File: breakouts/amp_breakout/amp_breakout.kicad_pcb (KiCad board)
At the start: 2 copper layers, 20 parts, among them P1 CONN_01X02, U1 CONN_SMA, U2 MGA-82563, U3 ADM7150, U4 CONN_SMA, U5 mounting_box

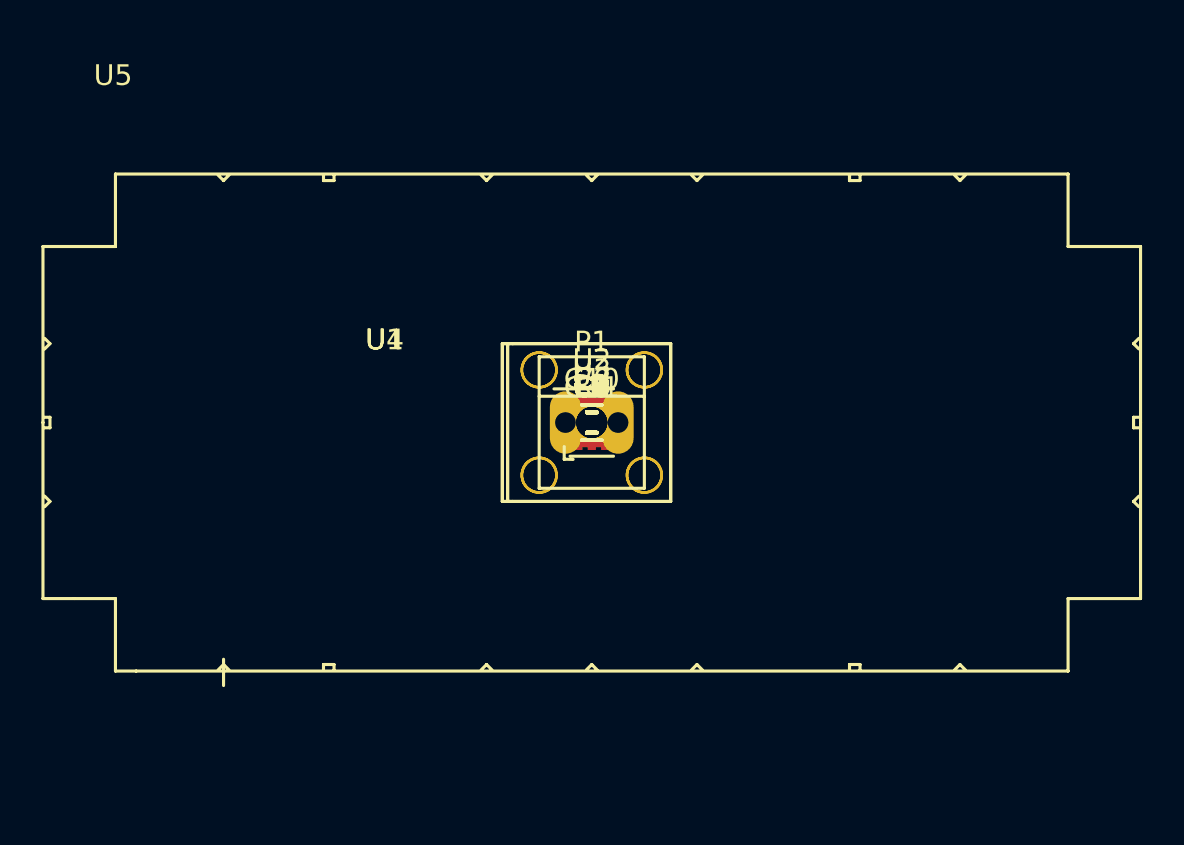
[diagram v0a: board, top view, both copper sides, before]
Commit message: started variable attenuator, revised synth, and added power splittert to detect board
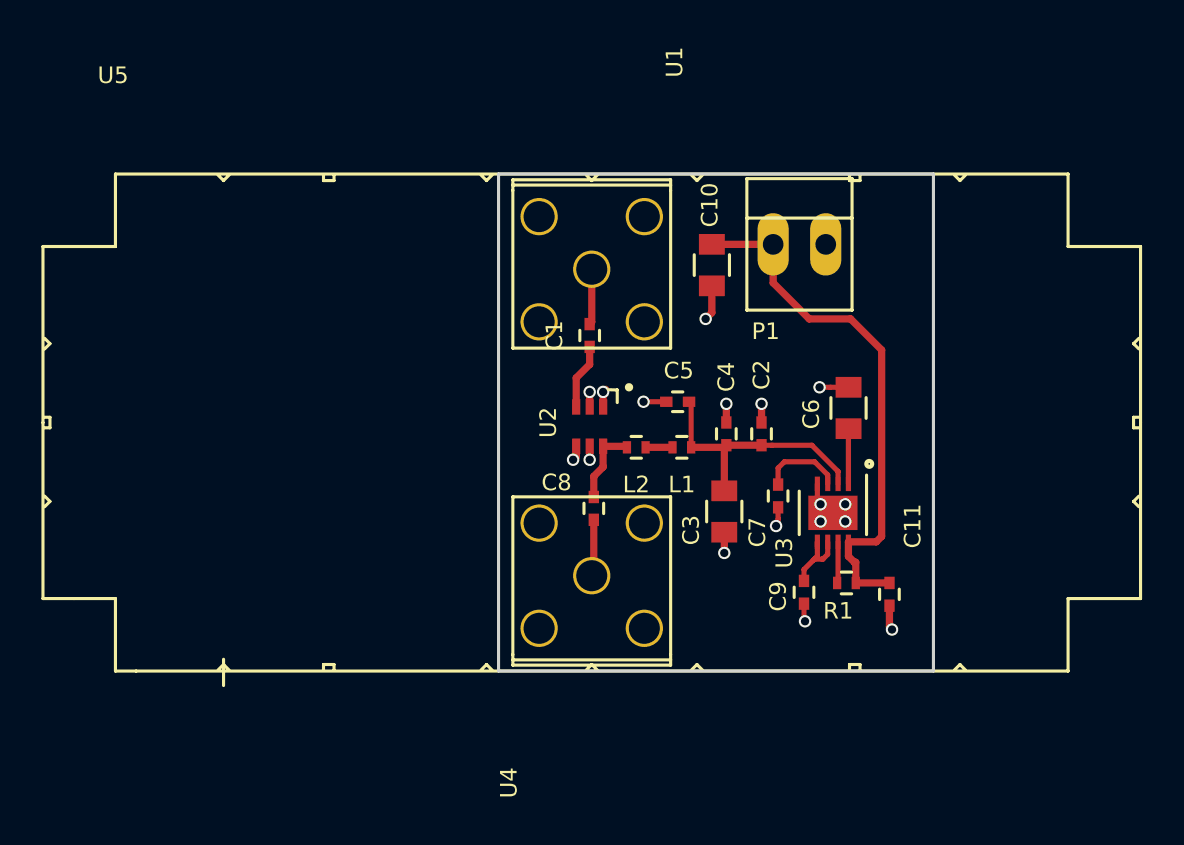
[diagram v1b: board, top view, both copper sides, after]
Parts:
- moved C11 16.6 mm to (162.9, 113.3), turned to 90 degrees
- moved R1 14.5 mm to (160.8, 112.8), turned to 180 degrees
- moved P1 13.2 mm to (158.5, 96.4)
- moved C9 13.1 mm to (158.8, 113.2), turned to 90 degrees
- moved U3 12.4 mm to (160.1, 109.4), turned to 270 degrees
- moved C6 12.4 mm to (160.9, 104.3), turned to 270 degrees
- moved C7 9.67 mm to (157.5, 108.5), turned to 90 degrees
- moved C10 9.56 mm to (154.3, 97.4), turned to 90 degrees
- moved C2 8.22 mm to (156.7, 105.5), turned to 270 degrees
- moved C3 7.71 mm to (154.9, 109.3), turned to 90 degrees
- moved U1 7.40 mm to (148.5, 97.6), turned to 270 degrees
- moved U4 7.40 mm to (148.5, 112.4), turned to 90 degrees
- moved C4 6.52 mm to (155.0, 105.5), turned to 270 degrees
- moved L1 4.51 mm to (152.8, 106.2), turned to 180 degrees
- moved C5 4.27 mm to (152.7, 104.0)
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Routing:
- net Net-(C10-Pad2): track 0.00 -> 25.9 mm
- net GND: track 0.00 -> 14.1 mm, vias 0 -> 17
- net Net-(C2-Pad2): track 0.00 -> 12.6 mm
- net Net-(C7-Pad2): track 0.00 -> 4.01 mm
- net Net-(C9-Pad2): track 0.00 -> 3.82 mm
- net Net-(C8-Pad2): track 0.00 -> 3.81 mm
- net Net-(C1-Pad1): track 0.00 -> 3.17 mm
- net Net-(C8-Pad1): track 0.00 -> 2.74 mm
- net Net-(C1-Pad2): track 0.00 -> 2.69 mm
- net Net-(C6-Pad2): track 0.00 -> 2.67 mm
- net Net-(R1-Pad2): track 0.00 -> 2.00 mm
- net Net-(L1-Pad2): track 0.00 -> 1.30 mm
- added copper zone on In1.Cu, net GND
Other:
- board outline added: 21 x 24 mm
- copper layers 2 -> 4
- net class Default: clearance 0.2 -> 0.13
- rule trace_clearance: 0.2 -> 0.13
- board text added: "2016.3"

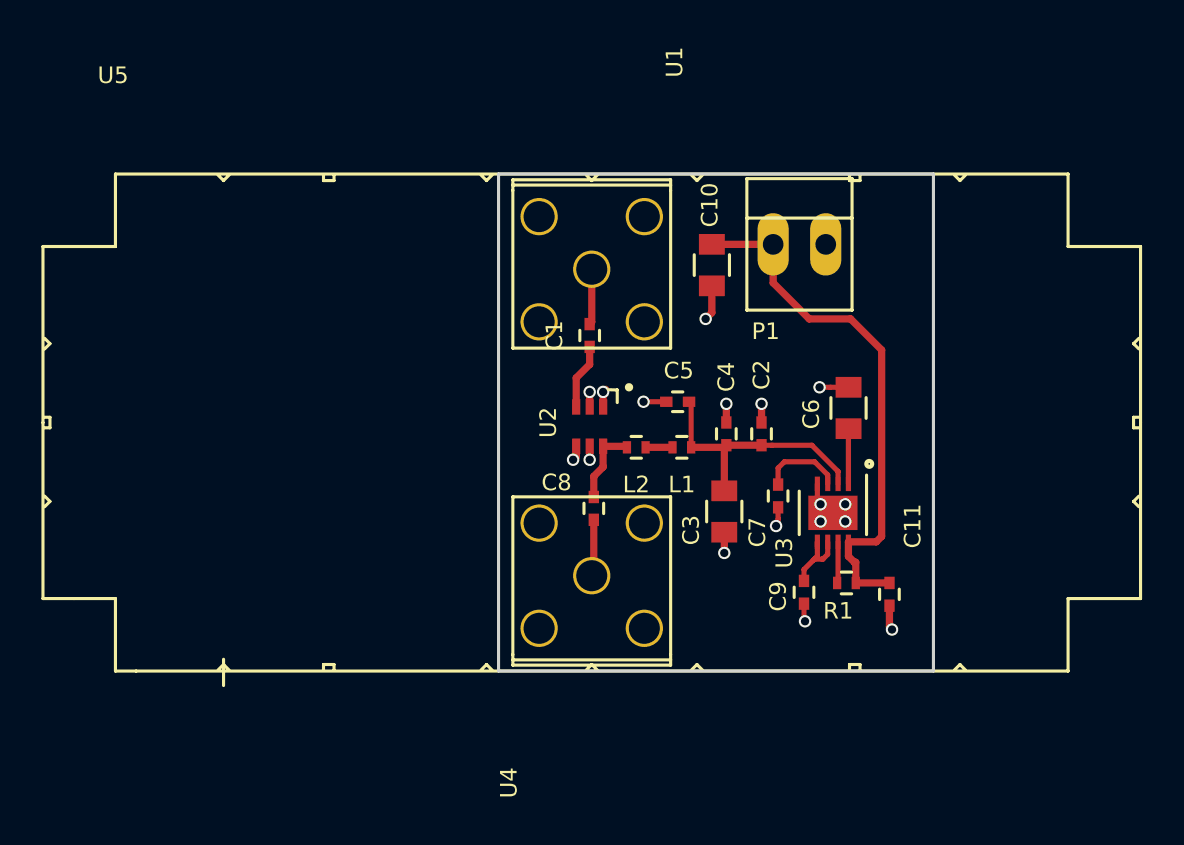
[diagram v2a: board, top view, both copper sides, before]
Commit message: changed sma connectors on amp board to edge launch, trimmed excess ground plane
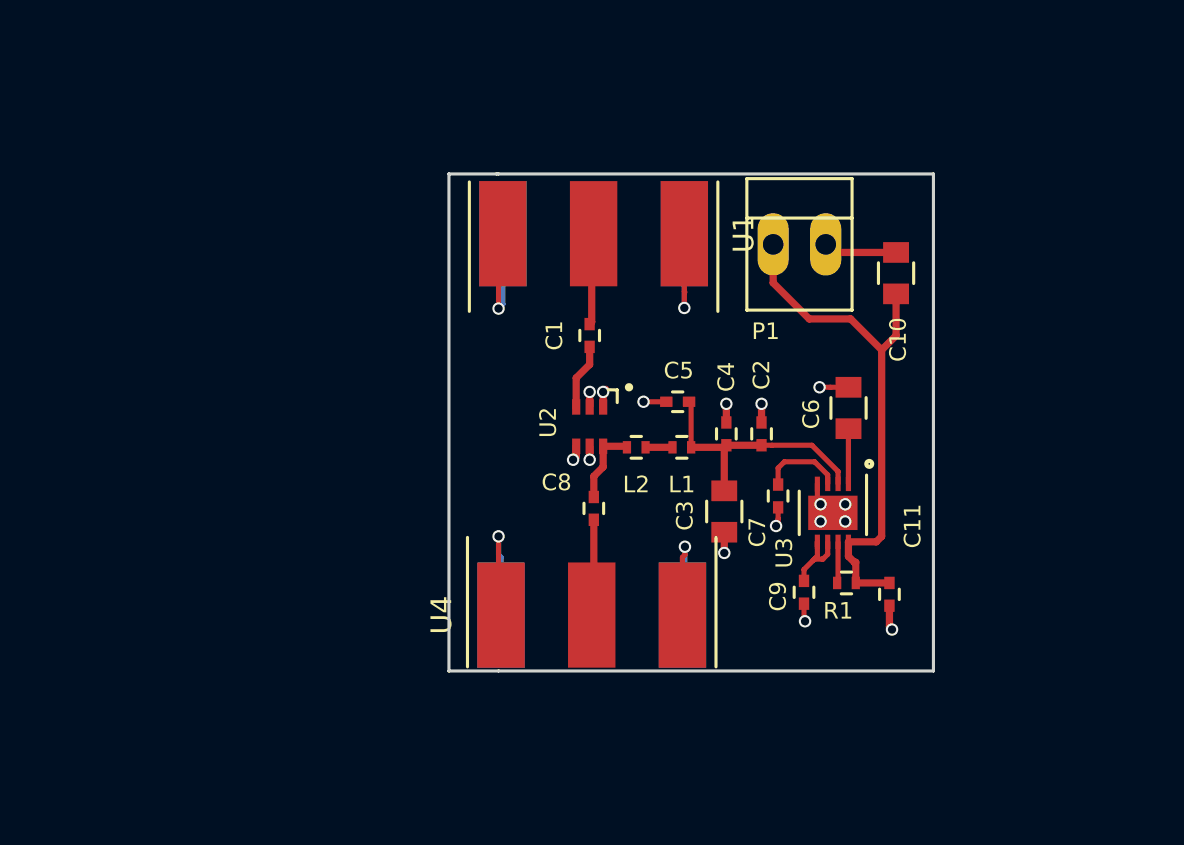
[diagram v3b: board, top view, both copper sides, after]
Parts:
- removed U5: mounting_box, vna_footprints:POMONA_2400BOX
- U1, U4: footprint vna_footprints:732512200_SMA -> vna_footprints:732511150_sma
- moved C10 8.90 mm to (163.2, 97.8), turned to 270 degrees
- moved U4 1.90 mm to (148.5, 114.3), turned to 0 degrees
- moved U1 1.72 mm to (148.6, 95.9), turned to 180 degrees
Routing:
- net GND: track 14.1 -> 44.9 mm, vias 17 -> 20
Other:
- board size 21 x 24 mm -> 23.4 x 24 mm
